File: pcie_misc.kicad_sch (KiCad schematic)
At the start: 42 parts, among them U37 9DBL0651CKILF, U38 74AUP2G132, Y1 Oscillator_32.768kHz_ECS_2520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

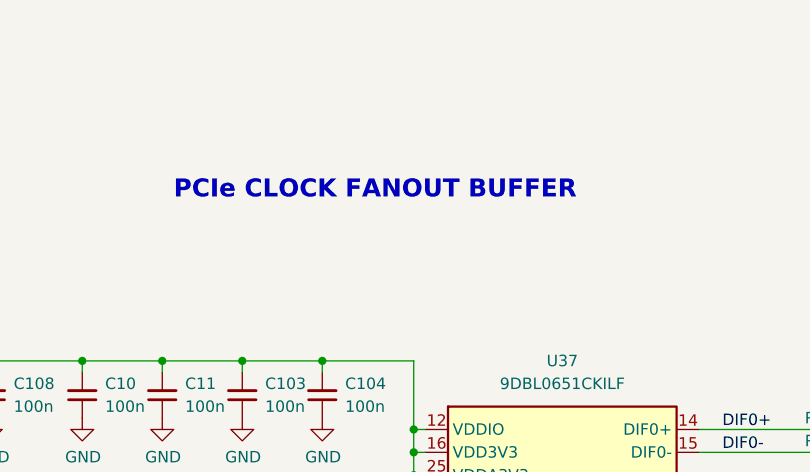
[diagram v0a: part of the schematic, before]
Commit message: [#70030] Unify functional block names
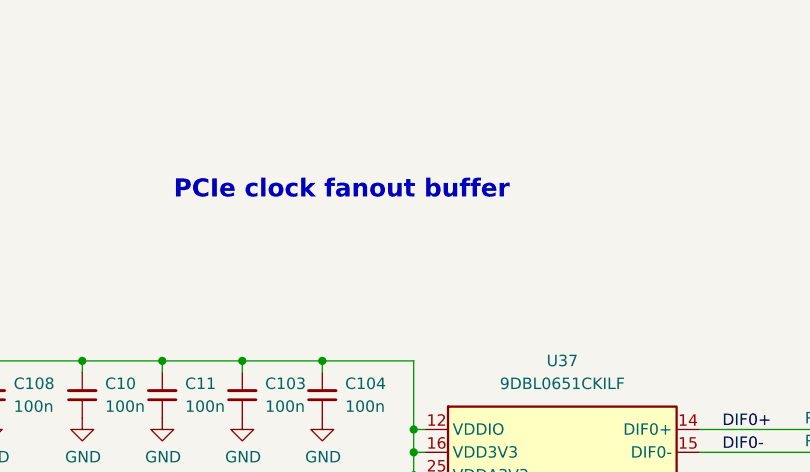
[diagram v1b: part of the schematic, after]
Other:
- note added: "PCIe clock fanout buffer"
- note removed: "PCIe CLOCK FANOUT BUFFER"
- company: Antmicro Ltd. -> Antmicro Ltd
- title: Com Express 7 baseboard -> COM Express 7 Baseboard
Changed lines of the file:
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@@
 	(paper "A3")
 	(title_block
-		(title "Com Express 7 baseboard")
-		(date "2024-03-28")
+		(title "COM Express 7 Baseboard")
+		(date "2024-12-13")
 		(rev "1.1.0")
-		(company "Antmicro Ltd.")
+		(company "Antmicro Ltd")
+		(comment 1 "www.antmicro.com")
 	)
 	(junction
@@
 		)
 	)
-	(text "PCIe CLOCK FANOUT BUFFER"
+	(text "PCIe clock fanout buffer"
 		(exclude_from_sim no)
 		(at 83.82 33.02 0)

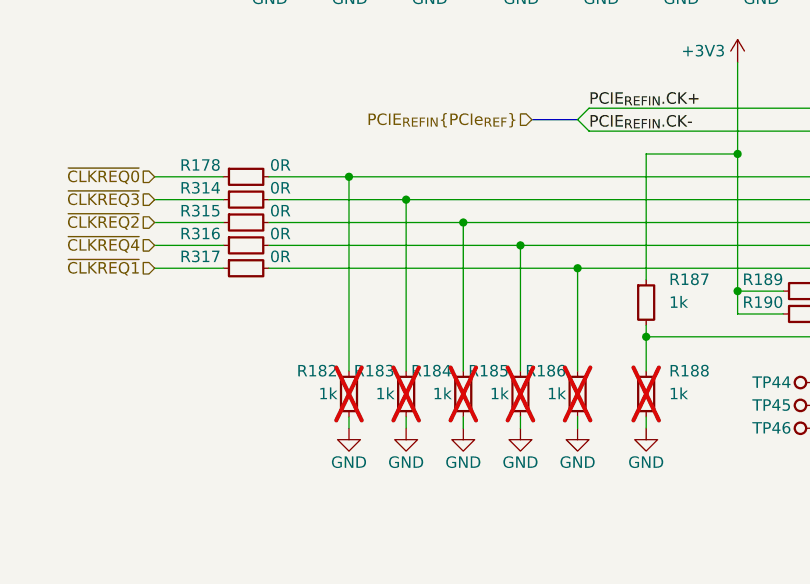
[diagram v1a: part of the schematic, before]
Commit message: [#70532] Enable all PCIe clock outputs with resistors
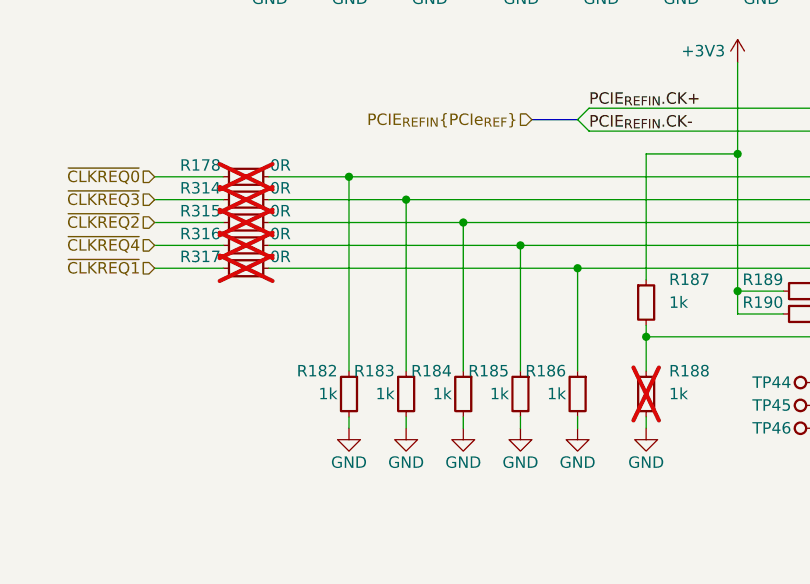
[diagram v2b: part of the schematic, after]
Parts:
- R178, R314, R315, R316, R317: now not fitted
- R182, R183, R184, R185, R186: now fitted
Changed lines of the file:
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@@
 		(in_bom yes)
 		(on_board yes)
-		(dnp no)
+		(dnp yes)
 		(property "Reference" "R178"
 			(at 38.1 80.01 0)
@@
 		(in_bom yes)
 		(on_board yes)
-		(dnp no)
+		(dnp yes)
 		(property "Reference" "R315"
 			(at 38.1 85.09 0)
@@
 		(in_bom yes)
 		(on_board yes)
-		(dnp no)
+		(dnp yes)
 		(property "Reference" "R317"
 			(at 38.1 90.17 0)
@@
 		(in_bom yes)
 		(on_board yes)
-		(dnp yes)
+		(dnp no)
 		(property "Reference" "R182"
 			(at 53.34 102.87 90)
@@
 		(in_bom yes)
 		(on_board yes)
-		(dnp yes)
+		(dnp no)
 		(property "Reference" "R185"
 			(at 72.39 102.87 90)
@@
 		(in_bom yes)
 		(on_board yes)
-		(dnp no)
+		(dnp yes)
 		(property "Reference" "R314"
 			(at 38.1 82.55 0)
@@
 		(in_bom yes)
 		(on_board yes)
-		(dnp yes)
+		(dnp no)
 		(property "Reference" "R184"
 			(at 66.04 102.87 90)
@@
 		(in_bom yes)
 		(on_board yes)
-		(dnp yes)
+		(dnp no)
 		(property "Reference" "R186"
 			(at 78.74 102.87 90)
@@
 		(in_bom yes)
 		(on_board yes)
-		(dnp no)
+		(dnp yes)
 		(property "Reference" "R316"
 			(at 38.1 87.63 0)
@@
 		(in_bom yes)
 		(on_board yes)
-		(dnp yes)
+		(dnp no)
 		(property "Reference" "R183"
 			(at 59.69 102.87 90)
